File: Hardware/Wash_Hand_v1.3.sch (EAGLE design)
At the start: 58 parts, among them IC1 LM358D, IC2 LP298XS, IC3 4050D, J1 I2C, J2 ICSP, J3 SPI, J5 EXT_VCC, J6 6_PIN_SERIAL_CABLEPTH, Q1 16.0 Mhz, U1 328P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

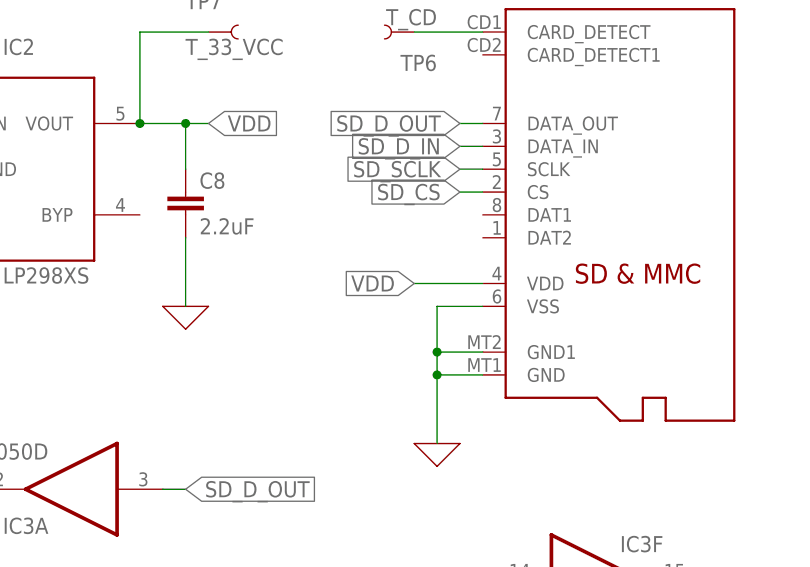
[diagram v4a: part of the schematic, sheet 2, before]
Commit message: Board: Move parts around so capacitors are close to LP298 and MIC52055
Both specs say that capacitors have to be within 0.5 inch.

Signed-off-by: Konrad Rzeszutek Wilk <konrad@kernel.org>
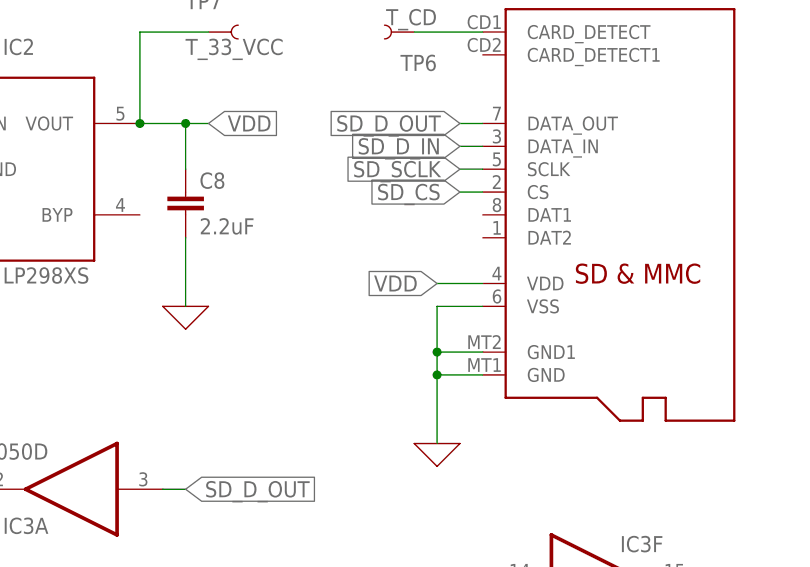
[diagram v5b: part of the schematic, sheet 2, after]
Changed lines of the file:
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@@
 <net name="VDD" class="0">
-<segment>
-<pinref part="U$7" gate="G$1" pin="VDD"/>
-<wire x1="81.28" y1="144.78" x2="73.66" y2="144.78" width="0.1524" layer="91"/>
-<label x="73.66" y="144.78" size="1.778" layer="95" rot="R180" xref="yes"/>
-</segment>
 <segment>
 <pinref part="IC2" gate="G$1" pin="VOUT"/>
@@
 <label x="96.52" y="88.9" size="1.778" layer="95" xref="yes"/>
 </segment>
+<segment>
+<pinref part="U$7" gate="G$1" pin="VDD"/>
+<wire x1="81.28" y1="144.78" x2="76.2" y2="144.78" width="0.1524" layer="91"/>
+<label x="76.2" y="144.78" size="1.778" layer="95" rot="R180" xref="yes"/>
+</segment>
 </net>

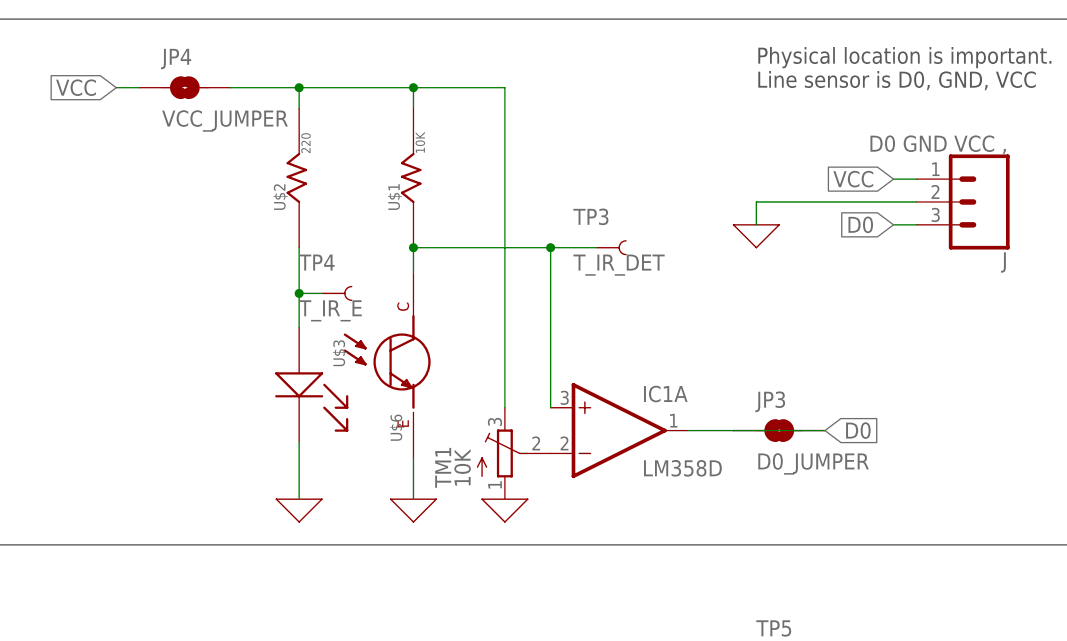
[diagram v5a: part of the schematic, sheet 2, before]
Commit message: Board: Rename VCC_JUMPER to EN_INT_SENSOR, D0_JUMPER, EN_INT_D0, and..
.. move copyright and such around.

Also add a text field around test spots.

Signed-off-by: Konrad Rzeszutek Wilk <konrad@kernel.org>
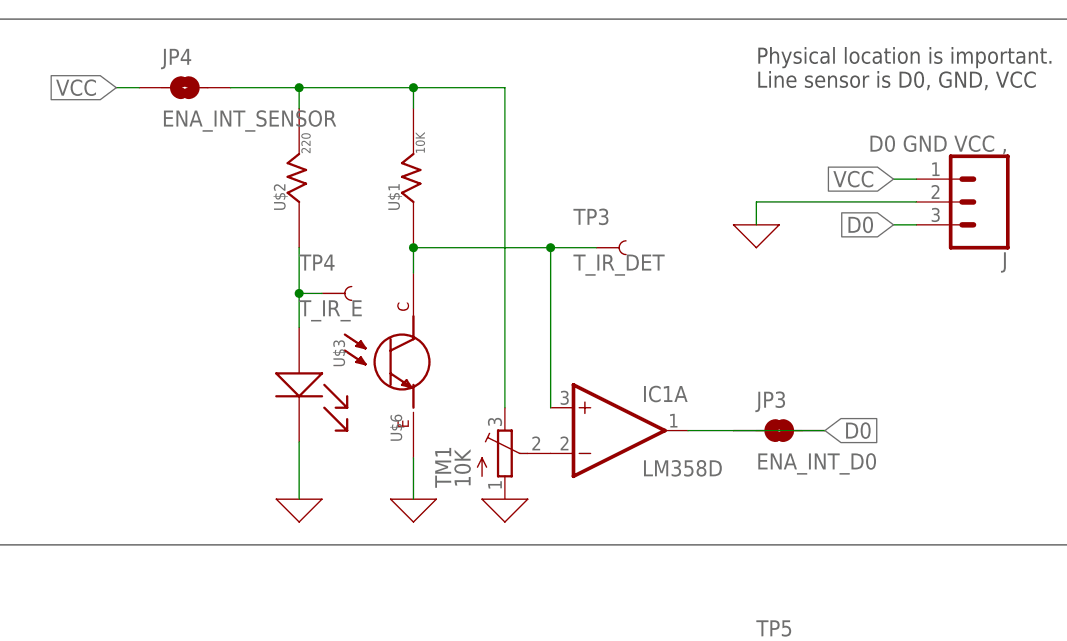
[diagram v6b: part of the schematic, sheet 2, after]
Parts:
- JP3: value D0_JUMPER -> ENA_INT_D0
- JP4: value VCC_JUMPER -> ENA_INT_SENSOR
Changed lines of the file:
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@@
 <part name="X_13" library="ngspice-simulation" library_urn="urn:adsk.eagle:library:527439" deviceset="GND" device=""/>
 <part name="JP2" library="SparkFun-Jumpers" library_urn="urn:adsk.eagle:library:528" deviceset="JUMPER-SMT_3_1-NC_PASTE" device="_SILK" package3d_urn="urn:adsk.eagle:package:39293/1" value="9V_JUMPER"/>
-<part name="JP3" library="SparkFun-Jumpers" library_urn="urn:adsk.eagle:library:528" deviceset="JUMPER-SMT_2_NO" device="_NO-SILK_ROUND" package3d_urn="urn:adsk.eagle:package:39278/1" value="D0_JUMPER"/>
-<part name="JP4" library="SparkFun-Jumpers" library_urn="urn:adsk.eagle:library:528" deviceset="JUMPER-SMT_2_NO" device="_NO-SILK_ROUND" package3d_urn="urn:adsk.eagle:package:39278/1" value="VCC_JUMPER"/>
+<part name="JP3" library="SparkFun-Jumpers" library_urn="urn:adsk.eagle:library:528" deviceset="JUMPER-SMT_2_NO" device="_NO-SILK_ROUND" package3d_urn="urn:adsk.eagle:package:39278/1" value="ENA_INT_D0"/>
+<part name="JP4" library="SparkFun-Jumpers" library_urn="urn:adsk.eagle:library:528" deviceset="JUMPER-SMT_2_NO" device="_NO-SILK_ROUND" package3d_urn="urn:adsk.eagle:package:39278/1" value="ENA_INT_SENSOR"/>
 <part name="U$1" library="darnok_common" deviceset="RESISTOR" device="R1206" value="10K"/>
 <part name="X_14" library="ngspice-simulation" library_urn="urn:adsk.eagle:library:527439" deviceset="GND" device=""/>

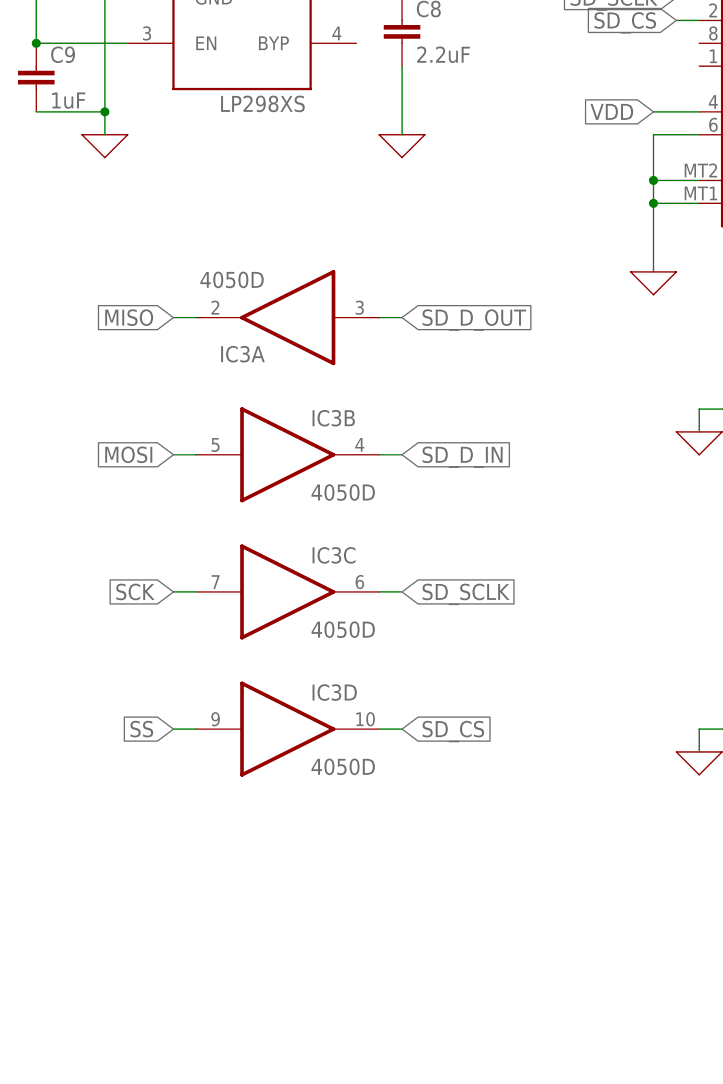
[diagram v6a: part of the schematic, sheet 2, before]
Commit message: Board: Added pull-up resistor for MISO(D0) line.
Various pages mention this is needed..?

Signed-off-by: Konrad Rzeszutek Wilk <konrad@kernel.org>
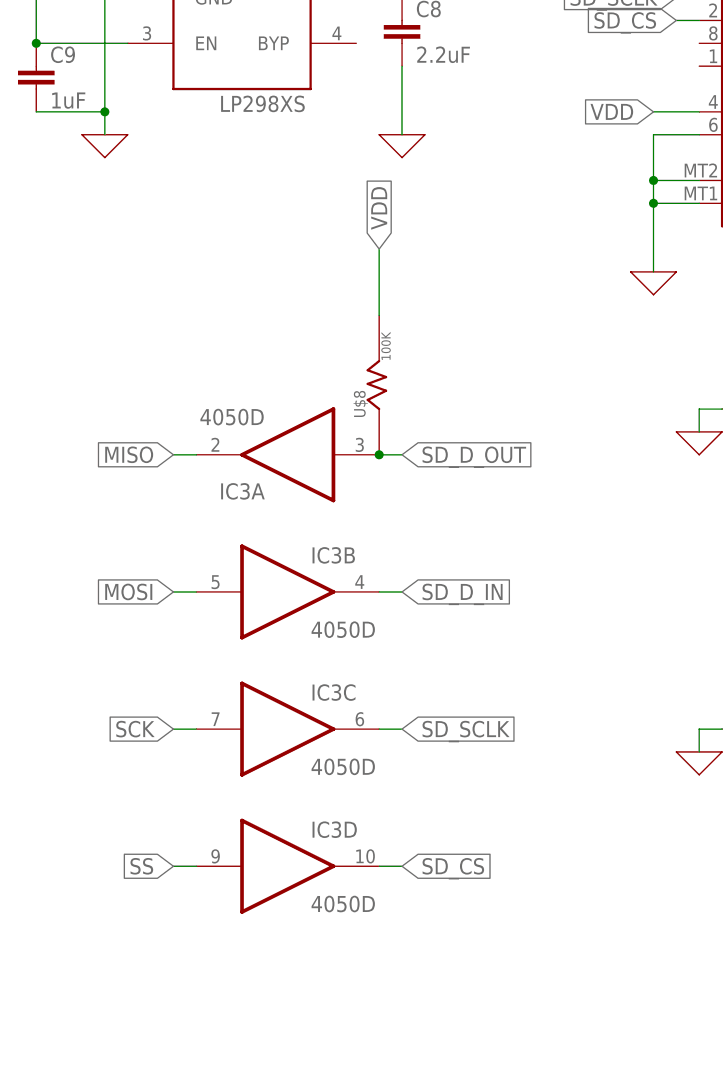
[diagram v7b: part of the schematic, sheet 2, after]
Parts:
- added U$8: 100K, darnok_common:RESISTORR1206
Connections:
- net SD_D_OUT: now also U$8.R_1
- net VDD: now also U$8.R_2
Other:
- moved on the sheet: IC3A, IC3B, IC3C, IC3D
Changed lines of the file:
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@@
 <part name="C9" library="SparkFun-Capacitors" library_urn="urn:adsk.eagle:library:510" deviceset="1.0UF" device="-1206-50V-10%" package3d_urn="urn:adsk.eagle:package:37426/1" value="1uF"/>
 <part name="X_24" library="ngspice-simulation" library_urn="urn:adsk.eagle:library:527439" deviceset="GND" device=""/>
+<part name="U$8" library="darnok_common" deviceset="RESISTOR" device="R1206" value="100K"/>
 </parts>
 <sheets>
@@
 <attribute name="VALUE" x="27.94" y="144.78" size="1.778" layer="96"/>
 </instance>
-<instance part="IC3" gate="A" x="35.56" y="121.92" smashed="yes" rot="R180">
-<attribute name="NAME" x="33.02" y="118.745" size="1.778" layer="95" rot="R180"/>
-<attribute name="VALUE" x="33.02" y="127" size="1.778" layer="96" rot="R180"/>
-</instance>
-<instance part="IC3" gate="B" x="35.56" y="106.68" smashed="yes">
-<attribute name="NAME" x="38.1" y="109.855" size="1.778" layer="95"/>
-<attribute name="VALUE" x="38.1" y="101.6" size="1.778" layer="96"/>
-</instance>
-<instance part="IC3" gate="C" x="35.56" y="91.44" smashed="yes">
+<instance part="IC3" gate="A" x="35.56" y="106.68" smashed="yes" rot="R180">
+<attribute name="NAME" x="33.02" y="103.505" size="1.778" layer="95" rot="R180"/>
+<attribute name="VALUE" x="33.02" y="111.76" size="1.778" layer="96" rot="R180"/>
+</instance>
+<instance part="IC3" gate="B" x="35.56" y="91.44" smashed="yes">
 <attribute name="NAME" x="38.1" y="94.615" size="1.778" layer="95"/>
 <attribute name="VALUE" x="38.1" y="86.36" size="1.778" layer="96"/>
 </instance>
-<instance part="IC3" gate="D" x="35.56" y="76.2" smashed="yes">
+<instance part="IC3" gate="C" x="35.56" y="76.2" smashed="yes">
 <attribute name="NAME" x="38.1" y="79.375" size="1.778" layer="95"/>
 <attribute name="VALUE" x="38.1" y="71.12" size="1.778" layer="96"/>
+</instance>
+<instance part="IC3" gate="D" x="35.56" y="60.96" smashed="yes">
+<attribute name="NAME" x="38.1" y="64.135" size="1.778" layer="95"/>
+<attribute name="VALUE" x="38.1" y="55.88" size="1.778" layer="96"/>
 </instance>
 <instance part="IC3" gate="E" x="93.98" y="76.2" smashed="yes">
@@
 </instance>
 <instance part="X_24" gate="G$1" x="48.26" y="142.24" smashed="yes"/>
+<instance part="U$8" gate="G$1" x="45.72" y="111.76" smashed="yes" rot="R90">
+<attribute name="NAME" x="44.196" y="110.744" size="1.27" layer="95" rot="R90"/>
+<attribute name="VALUE" x="46.99" y="117.094" size="1.016" layer="96" rot="R90"/>
+</instance>
 </instances>
 <busses>
@@
 <segment>
 <pinref part="IC3" gate="A" pin="I"/>
-<wire x1="45.72" y1="121.92" x2="48.26" y2="121.92" width="0.1524" layer="91"/>
-<label x="48.26" y="121.92" size="1.778" layer="95" xref="yes"/>
+<wire x1="45.72" y1="106.68" x2="48.26" y2="106.68" width="0.1524" layer="91"/>
+<label x="48.26" y="106.68" size="1.778" layer="95" xref="yes"/>
+<pinref part="U$8" gate="G$1" pin="R_1"/>
+<junction x="45.72" y="106.68"/>
 </segment>
 </net>
@@
 <segment>
 <pinref part="IC3" gate="B" pin="O"/>
-<wire x1="45.72" y1="106.68" x2="48.26" y2="106.68" width="0.1524" layer="91"/>
-<label x="48.26" y="106.68" size="1.778" layer="95" xref="yes"/>
+<wire x1="45.72" y1="91.44" x2="48.26" y2="91.44" width="0.1524" layer="91"/>
+<label x="48.26" y="91.44" size="1.778" layer="95" xref="yes"/>
 </segment>
 </net>
@@
 <segment>
 <pinref part="IC3" gate="C" pin="O"/>
-<wire x1="45.72" y1="91.44" x2="48.26" y2="91.44" width="0.1524" layer="91"/>
-<label x="48.26" y="91.44" size="1.778" layer="95" xref="yes"/>
+<wire x1="45.72" y1="76.2" x2="48.26" y2="76.2" width="0.1524" layer="91"/>
+<label x="48.26" y="76.2" size="1.778" layer="95" xref="yes"/>
 </segment>
 </net>
@@
 <segment>
 <pinref part="IC3" gate="D" pin="O"/>
-<wire x1="45.72" y1="76.2" x2="48.26" y2="76.2" width="0.1524" layer="91"/>
-<label x="48.26" y="76.2" size="1.778" layer="95" xref="yes"/>
+<wire x1="45.72" y1="60.96" x2="48.26" y2="60.96" width="0.1524" layer="91"/>
+<label x="48.26" y="60.96" size="1.778" layer="95" xref="yes"/>
 </segment>
 </net>
@@
 <label x="76.2" y="144.78" size="1.778" layer="95" rot="R180" xref="yes"/>
 </segment>
+<segment>
+<pinref part="U$8" gate="G$1" pin="R_2"/>
+<wire x1="45.72" y1="122.174" x2="45.72" y2="129.54" width="0.1524" layer="91"/>
+<label x="45.72" y="129.54" size="1.778" layer="95" rot="R90" xref="yes"/>
+</segment>
 </net>
 <net name="N$17" class="0">
@@
 <segment>
 <pinref part="IC3" gate="D" pin="I"/>
+<wire x1="25.4" y1="60.96" x2="22.86" y2="60.96" width="0.1524" layer="91"/>
+<label x="22.86" y="60.96" size="1.778" layer="95" rot="R180" xref="yes"/>
+</segment>
+</net>
+<net name="SCK" class="0">
+<segment>
+<pinref part="IC3" gate="C" pin="I"/>
 <wire x1="25.4" y1="76.2" x2="22.86" y2="76.2" width="0.1524" layer="91"/>
 <label x="22.86" y="76.2" size="1.778" layer="95" rot="R180" xref="yes"/>
 </segment>
 </net>
-<net name="SCK" class="0">
-<segment>
-<pinref part="IC3" gate="C" pin="I"/>
+<net name="MOSI" class="0">
+<segment>
+<pinref part="IC3" gate="B" pin="I"/>
 <wire x1="25.4" y1="91.44" x2="22.86" y2="91.44" width="0.1524" layer="91"/>
 <label x="22.86" y="91.44" size="1.778" layer="95" rot="R180" xref="yes"/>
 </segment>
 </net>
-<net name="MOSI" class="0">
-<segment>
-<pinref part="IC3" gate="B" pin="I"/>
+<net name="MISO" class="0">
+<segment>
+<pinref part="IC3" gate="A" pin="O"/>
 <wire x1="25.4" y1="106.68" x2="22.86" y2="106.68" width="0.1524" layer="91"/>
 <label x="22.86" y="106.68" size="1.778" layer="95" rot="R180" xref="yes"/>
 </segment>
 </net>
-<net name="MISO" class="0">
-<segment>
-<pinref part="IC3" gate="A" pin="O"/>
-<wire x1="25.4" y1="121.92" x2="22.86" y2="121.92" width="0.1524" layer="91"/>
-<label x="22.86" y="121.92" size="1.778" layer="95" rot="R180" xref="yes"/>
-</segment>
-</net>
